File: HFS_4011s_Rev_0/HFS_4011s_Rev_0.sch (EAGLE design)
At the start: 63 parts, among them IC1 CP2104, J1 2X06, J2 2X12, J3 1X02, J4 microUSB, J5 1X02, J6 MOLEX_IGRID_15X2CONNECTOR, Q1 mmbt2222, Q2 mmbt2222, Q3 MMUN2133LT1G, Q4 BSS138, Q5 BSS138, SW2 KMR2, U1 TPS61090RSAR, U2 MCP73831T-2ACI/OT, U3 AD5693R, U4 LM3671MF-3.3/NOPB, X2 ESP32_WROOM32_SKINNY

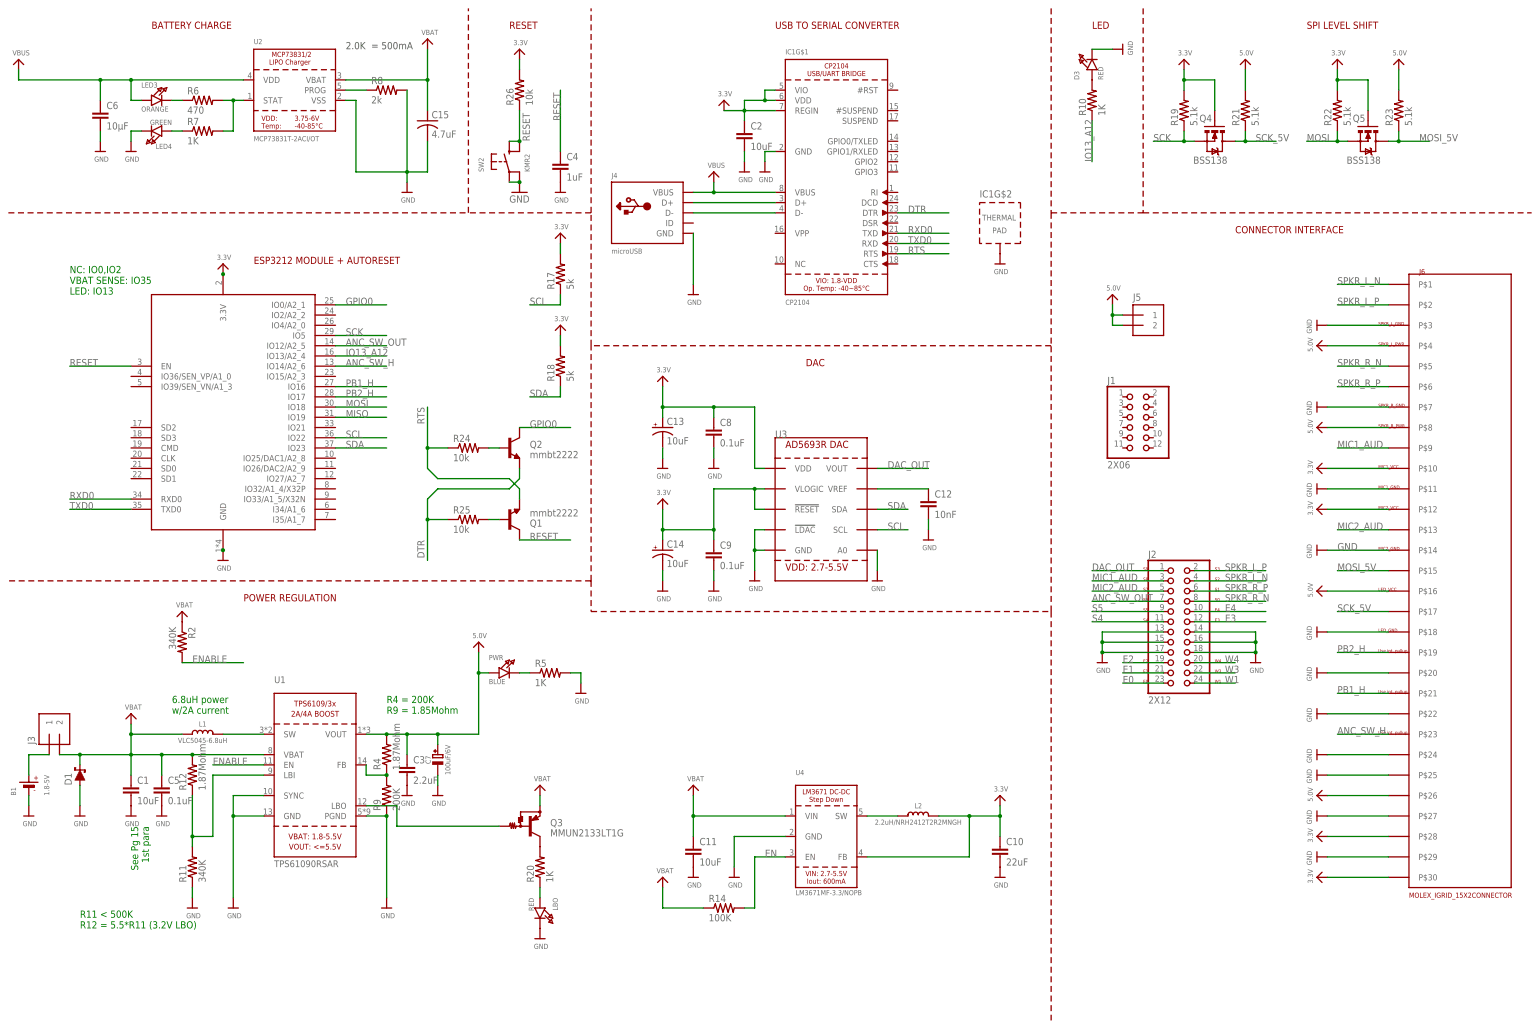
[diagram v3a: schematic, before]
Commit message: Renumbered components and fixing DRC errors.
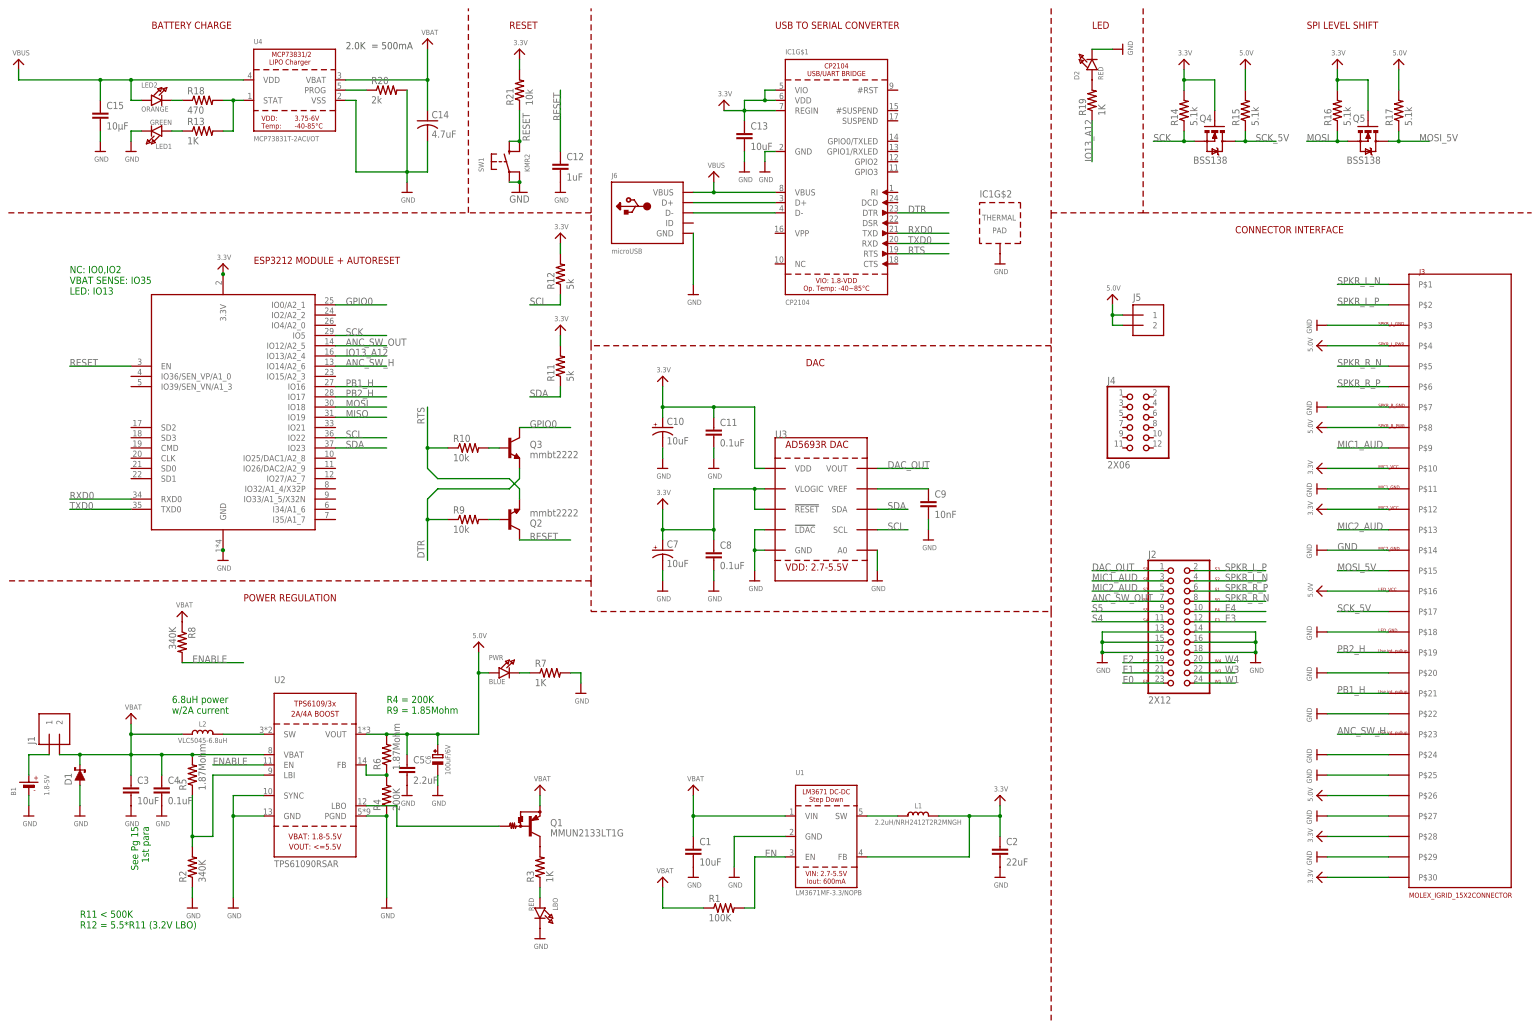
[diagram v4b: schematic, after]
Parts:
- removed R23: 5.1k, rcl:R-US_R0603
- removed R24, R25, R26: 10k, rcl:R-US_R0603
- added R1: 100K, rcl:R-US_R0603
- added R13, R3: 1K, rcl:R-US_R0603
- added R15: 5.1k, rcl:R-US_R0603
- C10: value 22uF -> 10uF; device rcl:C-EUC0603 -> SparkFun-Retired:10UF-TANT
- C11: value 10uF -> 0.1uF
- C12: value 10nF -> 1uF
- C13: device SparkFun-Retired:10UF-TANT -> rcl:C-EUC0603
- C14: value 10uF -> 4.7uF; device SparkFun-Retired:10UF-TANT -> rcl:C-USC1206
- C15: value 4.7uF -> 10µF; device rcl:C-USC1206 -> rcl:C-EUC0603
- C2: value 10uF -> 22uF
- C3: value 2.2uF -> 10uF
- C4: value 1uF -> 0.1uF
- C5: value 0.1uF -> 2.2uF
- C6: value 10µF -> 100uF/6V; device rcl:C-EUC0603 -> microbuilder:CAP_TANTALUMB/3528_REFLOW
- C7: value 100uF/6V -> 10uF; device microbuilder:CAP_TANTALUMB/3528_REFLOW -> SparkFun-Retired:10UF-TANT
- C9: value 0.1uF -> 10nF
- J1: value 2X06 -> 1X02; device HFS4011sCustom:2X06 -> HFS4011sCustom:1X02
- J3: value 1X02 -> MOLEX_IGRID_15X2CONNECTOR; device HFS4011sCustom:1X02 -> HFS4011sCustom:MOLEX_IGRID_15X2CONNECTOR
- J4: value microUSB -> 2X06; device microbuilder:USBMICRO_20329 -> HFS4011sCustom:2X06
- J6: value MOLEX_IGRID_15X2CONNECTOR -> microUSB; device HFS4011sCustom:MOLEX_IGRID_15X2CONNECTOR -> microbuilder:USBMICRO_20329
- L1: value VLC5045-6.8uH -> 2.2uH/NRH2412T2R2MNGH; device microbuilder:INDUCTORTDK_VLC5045 -> microbuilder:INDUCTORNRH2412T
- L2: value 2.2uH/NRH2412T2R2MNGH -> VLC5045-6.8uH; device microbuilder:INDUCTORNRH2412T -> microbuilder:INDUCTORTDK_VLC5045
- Q1: value mmbt2222 -> MMUN2133LT1G; device SparkFun:TRANSISTOR_NPNSOT23-3 -> transistor:MUN2114T1-PNP_DRIVER-SC59-BEC
- Q3: value MMUN2133LT1G -> mmbt2222; device transistor:MUN2114T1-PNP_DRIVER-SC59-BEC -> SparkFun:TRANSISTOR_NPNSOT23-3
- R10: value 1K -> 10k
- R11: value 340K -> 5k
- R12: value 1.87Mohm -> 5k
- R14: value 100K -> 5.1k
- R17: value 5k -> 5.1k
- R18: value 5k -> 470
- R19: value 5.1k -> 1K
- R20: value 1K -> 2k
- R21: value 5.1k -> 10k
- R4: value 1.87Mohm -> 200K
- R5: value 1K -> 1.87Mohm
- R6: value 470 -> 1.87Mohm
- R8: value 2k -> 340K
- R9: value 200K -> 10k
- U1: value TPS61090RSAR -> LM3671MF-3.3/NOPB; device microbuilder:VREG_TPS6103X -> microbuilder:VREG_LM3671
- U2: value MCP73831T-2ACI/OT -> TPS61090RSAR; device microbuilder:MCP73831/2 -> microbuilder:VREG_TPS6103X
- U4: value LM3671MF-3.3/NOPB -> MCP73831T-2ACI/OT; device microbuilder:VREG_LM3671 -> microbuilder:MCP73831/2
- renumbered D3 to D2, LED3 to LED2, LED4 to LED1, R22 to R16, SW2 to SW1, X2 to X1
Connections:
- net 3.3V: now also C10.+, C11.1, C13.1, C7.+, J3.P$10, J3.P$12, J3.P$28, J3.P$30, L1.2, R11.2, R12.2, R14.2, R21.2, U1.FB; no longer C10.1, C13.+, C14.+, C9.1, J6.P$10, J6.P$12, J6.P$28, J6.P$30, L2.2, R17.2, R18.2, R19.2, R26.2, U4.FB
- net 5.0V: now also C5.1, C6.+, J3.P$16, J3.P$26, J3.P$4, J3.P$8, R15.2, R17.2, R6.2, U2.VOUT; no longer C3.1, C7.+, J6.P$16, J6.P$26, J6.P$4, J6.P$8, R21.2, R23.2, R4.2, U1.VOUT
- net ANC_SW_H: now also J3.P$23; no longer J6.P$23
- net DTR: now also Q3.E, R9.1; no longer Q2.E, R25.1
- net EN: now also R1.2, U1.EN; no longer R14.2, U4.EN
- net ENABLE: now also R8.2, U2.EN; no longer R2.2, U1.EN
- net GND: now also C10.-, C13.2, C14.2, C6.-, J3.P$11, J3.P$14, J3.P$18, J3.P$20, J3.P$22, J3.P$24, J3.P$25, J3.P$27, J3.P$29, J3.P$3, J3.P$7, J6.GND, R2.1, R20.2, R4.1, R7.2, U2.GND, U2.PGND, U2.SYNC, U4.VSS; no longer C10.2, C13.-, C14.-, C6.2, J4.GND, J6.P$11, J6.P$14, J6.P$18, J6.P$20, J6.P$22, J6.P$24, J6.P$25, J6.P$27, J6.P$29, J6.P$3, J6.P$7, R11.1, R5.2, R8.2, R9.1, U1.PGND, U1.SYNC, U2.VSS, U4.GND
- net GPIO0: now also Q3.C; no longer Q2.C
- net IO13_A12: now also R19.1; no longer R10.1
- net LBO: now also Q1.B, U2.LBO; no longer Q3.B, U1.LBO
- net MIC1_AUD: now also J3.P$9; no longer J6.P$9
- net MIC2_AUD: now also J3.P$13; no longer J6.P$13
- net MOSI_5V: now also J3.P$15, R17.1; no longer J6.P$15, R23.1
- net N$1: now also R18.1; no longer R6.1
- net N$10: now also R7.1; no longer R5.1
- net N$11: now also R4.2, R6.1, U2.FB; no longer R4.1, R9.2, U1.FB
- net N$12: now also Q2.B, R9.2; no longer Q1.B, R25.2
- net N$13: now also Q3.B, R10.2; no longer Q2.B, R24.2
- net N$14: now also R3.1; no longer R20.1
- net N$15: now also Q1.C, R3.2; no longer Q3.C, R20.2
- net N$16: now also J1.1; no longer J3.1
- net N$17: now also L1.1, U1.SW; no longer L2.1, U4.SW
- net N$2: now also J6.D+; no longer J4.D+
- net N$20: now also C9.1; no longer C12.1
- net N$3: now also L2.2, U2.SW; no longer L1.2, U1.SW
- net N$4: now also R2.2, R5.1, U2.LBI; no longer R11.2, R12.1, U1.LBI
- net N$5: now also R19.2; no longer R10.2
- net N$6: now also J6.D-; no longer J4.D-
- net N$7: now also R13.2, R18.2, U4.STAT; no longer R6.2, R7.2, U2.STAT
- net N$8: now also R20.1, U4.PROG; no longer R8.1, U2.PROG
- net N$9: now also R13.1; no longer R7.1
- net PB1_H: now also J3.P$21; no longer J6.P$21
- net PB2_H: now also J3.P$19; no longer J6.P$19
- net RESET: now also C12.1, Q2.C, R21.1; no longer C4.1, Q1.C, R26.1
- net RTS: now also Q2.E, R10.1; no longer Q1.E, R24.1
- net SCK: now also R14.1; no longer R19.1
- net SCK_5V: now also J3.P$17, R15.1; no longer J6.P$17, R21.1
- net SCL: now also R12.1; no longer R17.1
- net SDA: now also R11.1; no longer R18.1
- net SPKR_L_N: now also J3.P$1; no longer J6.P$1
- net SPKR_L_P: now also J3.P$2; no longer J6.P$2
- net SPKR_R_N: now also J3.P$5; no longer J6.P$5
- net SPKR_R_P: now also J3.P$6; no longer J6.P$6
- net VBAT: now also C14.1, C3.1, C4.1, J1.2, L2.1, Q1.E, R1.1, R5.2, R8.1, U1.VIN, U4.VBAT; no longer C11.1, C15.1, C5.1, J3.2, L1.1, Q3.E, R12.2, R14.1, R2.1, U1.VBAT, U4.VIN
- net VBUS: now also C15.1, J6.VBUS, U4.VDD; no longer C6.1, J4.VBUS, U2.VDD
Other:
- moved on the sheet: C1, C11, C12, C15, C2, C3, C4, C5, C8, C9, L1, L2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

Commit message: Finished adding all silkscreen text. Got rid of some clearance errors. Seems like everything is set for fab.
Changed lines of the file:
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@@
 <grid distance="0.1" unitdist="inch" unit="inch" style="lines" multiple="1" display="no" altdistance="0.01" altunitdist="inch" altunit="inch"/>
 <layers>
-<layer number="1" name="Top" color="4" fill="1" visible="yes" active="no"/>
-<layer number="2" name="Route2" color="1" fill="3" visible="yes" active="no"/>
-<layer number="3" name="Route3" color="4" fill="3" visible="yes" active="no"/>
-<layer number="4" name="Route4" color="1" fill="4" visible="yes" active="no"/>
-<layer number="5" name="Route5" color="4" fill="4" visible="yes" active="no"/>
-<layer number="6" name="Route6" color="1" fill="8" visible="yes" active="no"/>
-<layer number="7" name="Route7" color="4" fill="8" visible="yes" active="no"/>
-<layer number="8" name="Route8" color="1" fill="2" visible="yes" active="no"/>
-<layer number="9" name="Route9" color="4" fill="2" visible="yes" active="no"/>
-<layer number="10" name="Route10" color="1" fill="7" visible="yes" active="no"/>
-<layer number="11" name="Route11" color="4" fill="7" visible="yes" active="no"/>
-<layer number="12" name="Route12" color="1" fill="5" visible="yes" active="no"/>
-<layer number="13" name="Route13" color="4" fill="5" visible="yes" active="no"/>
-<layer number="14" name="Route14" color="1" fill="6" visible="yes" active="no"/>
-<layer number="15" name="Route15" color="4" fill="6" visible="yes" active="no"/>
-<layer number="16" name="Bottom" color="1" fill="1" visible="yes" active="no"/>
-<layer number="17" name="Pads" color="2" fill="1" visible="yes" active="no"/>
-<layer number="18" name="Vias" color="2" fill="1" visible="yes" active="no"/>
-<layer number="19" name="Unrouted" color="6" fill="1" visible="yes" active="no"/>
-<layer number="20" name="Dimension" color="24" fill="1" visible="yes" active="no"/>
-<layer number="21" name="tPlace" color="7" fill="1" visible="yes" active="no"/>
-<layer number="22" name="bPlace" color="7" fill="1" visible="yes" active="no"/>
-<layer number="23" name="tOrigins" color="15" fill="1" visible="yes" active="no"/>
-<layer number="24" name="bOrigins" color="15" fill="1" visible="yes" active="no"/>
-<layer number="25" name="tNames" color="7" fill="1" visible="yes" active="no"/>
-<layer number="26" name="bNames" color="7" fill="1" visible="yes" active="no"/>
-<layer number="27" name="tValues" color="7" fill="1" visible="yes" active="no"/>
-<layer number="28" name="bValues" color="7" fill="1" visible="yes" active="no"/>
+<layer number="1" name="Top" color="4" fill="1" visible="no" active="no"/>
+<layer number="2" name="Route2" color="1" fill="3" visible="no" active="no"/>
+<layer number="3" name="Route3" color="4" fill="3" visible="no" active="no"/>
+<layer number="4" name="Route4" color="1" fill="4" visible="no" active="no"/>
+<layer number="5" name="Route5" color="4" fill="4" visible="no" active="no"/>
+<layer number="6" name="Route6" color="1" fill="8" visible="no" active="no"/>
+<layer number="7" name="Route7" color="4" fill="8" visible="no" active="no"/>
+<layer number="8" name="Route8" color="1" fill="2" visible="no" active="no"/>
+<layer number="9" name="Route9" color="4" fill="2" visible="no" active="no"/>
+<layer number="10" name="Route10" color="1" fill="7" visible="no" active="no"/>
+<layer number="11" name="Route11" color="4" fill="7" visible="no" active="no"/>
+<layer number="12" name="Route12" color="1" fill="5" visible="no" active="no"/>
+<layer number="13" name="Route13" color="4" fill="5" visible="no" active="no"/>
+<layer number="14" name="Route14" color="1" fill="6" visible="no" active="no"/>
+<layer number="15" name="Route15" color="4" fill="6" visible="no" active="no"/>
+<layer number="16" name="Bottom" color="1" fill="1" visible="no" active="no"/>
+<layer number="17" name="Pads" color="2" fill="1" visible="no" active="no"/>
+<layer number="18" name="Vias" color="2" fill="1" visible="no" active="no"/>
+<layer number="19" name="Unrouted" color="6" fill="1" visible="no" active="no"/>
+<layer number="20" name="Dimension" color="24" fill="1" visible="no" active="no"/>
+<layer number="21" name="tPlace" color="7" fill="1" visible="no" active="no"/>
+<layer number="22" name="bPlace" color="7" fill="1" visible="no" active="no"/>
+<layer number="23" name="tOrigins" color="15" fill="1" visible="no" active="no"/>
+<layer number="24" name="bOrigins" color="15" fill="1" visible="no" active="no"/>
+<layer number="25" name="tNames" color="7" fill="1" visible="no" active="no"/>
+<layer number="26" name="bNames" color="7" fill="1" visible="no" active="no"/>
+<layer number="27" name="tValues" color="7" fill="1" visible="no" active="no"/>
+<layer number="28" name="bValues" color="7" fill="1" visible="no" active="no"/>
 <layer number="29" name="tStop" color="7" fill="3" visible="no" active="no"/>
 <layer number="30" name="bStop" color="7" fill="6" visible="no" active="no"/>
@@
 <layer number="35" name="tGlue" color="7" fill="4" visible="no" active="no"/>
 <layer number="36" name="bGlue" color="7" fill="5" visible="no" active="no"/>
-<layer number="37" name="tTest" color="7" fill="1" visible="yes" active="no"/>
-<layer number="38" name="bTest" color="7" fill="1" visible="yes" active="no"/>
+<layer number="37" name="tTest" color="7" fill="1" visible="no" active="no"/>
+<layer number="38" name="bTest" color="7" fill="1" visible="no" active="no"/>
 <layer number="39" name="tKeepout" color="4" fill="11" visible="no" active="no"/>
 <layer number="40" name="bKeepout" color="1" fill="11" visible="no" active="no"/>
@@
 <layer number="44" name="Drills" color="7" fill="1" visible="no" active="no"/>
 <layer number="45" name="Holes" color="7" fill="1" visible="no" active="no"/>
-<layer number="46" name="Milling" color="3" fill="1" visible="yes" active="no"/>
-<layer number="47" name="Measures" color="7" fill="1" visible="yes" active="no"/>
-<layer number="48" name="Document" color="7" fill="1" visible="yes" active="no"/>
-<layer number="49" name="Reference" color="7" fill="1" visible="yes" active="no"/>
-<layer number="50" name="dxf" color="7" fill="1" visible="yes" active="no"/>
-<layer number="51" name="tDocu" color="7" fill="1" visible="yes" active="no"/>
-<layer number="52" name="bDocu" color="7" fill="1" visible="yes" active="no"/>
-<layer number="53" name="tGND_GNDA" color="7" fill="9" visible="yes" active="no"/>
-<layer number="54" name="bGND_GNDA" color="1" fill="9" visible="yes" active="no"/>
-<layer number="56" name="wert" color="7" fill="1" visible="yes" active="no"/>
-<layer number="57" name="tCAD" color="7" fill="1" visible="yes" active="no"/>
-<layer number="59" name="tCarbon" color="7" fill="1" visible="yes" active="no"/>
-<layer number="60" name="bCarbon" color="7" fill="1" visible="yes" active="no"/>
+<layer number="46" name="Milling" color="3" fill="1" visible="no" active="no"/>
+<layer number="47" name="Measures" color="7" fill="1" visible="no" active="no"/>
+<layer number="48" name="Document" color="7" fill="1" visible="no" active="no"/>
+<layer number="49" name="Reference" color="7" fill="1" visible="no" active="no"/>
+<layer number="50" name="dxf" color="7" fill="1" visible="no" active="no"/>
+<layer number="51" name="tDocu" color="7" fill="1" visible="no" active="no"/>
+<layer number="52" name="bDocu" color="7" fill="1" visible="no" active="no"/>
+<layer number="53" name="tGND_GNDA" color="7" fill="9" visible="no" active="no"/>
+<layer number="54" name="bGND_GNDA" color="1" fill="9" visible="no" active="no"/>
+<layer number="56" name="wert" color="7" fill="1" visible="no" active="no"/>
+<layer number="57" name="tCAD" color="7" fill="1" visible="no" active="no"/>
+<layer number="59" name="tCarbon" color="7" fill="1" visible="no" active="no"/>
+<layer number="60" name="bCarbon" color="7" fill="1" visible="no" active="no"/>
 <layer number="88" name="SimResults" color="9" fill="1" visible="yes" active="yes"/>
 <layer number="89" name="SimProbes" color="9" fill="1" visible="yes" active="yes"/>
@@
 <part name="R16" library="rcl" library_urn="urn:adsk.eagle:library:334" deviceset="R-US_" device="R0603" package3d_urn="urn:adsk.eagle:package:23555/2" value="5.1k"/>
 <part name="R17" library="rcl" library_urn="urn:adsk.eagle:library:334" deviceset="R-US_" device="R0603" package3d_urn="urn:adsk.eagle:package:23555/2" value="5.1k"/>
-<part name="J3" library="HFS4011sCustom" deviceset="MOLEX_IGRID_15X2CONNECTOR" device=""/>
+<part name="J3" library="HFS4011sCustom" deviceset="MOLEX_IGRID_15X2CONNECTOR" device="" value=""/>
 <part name="U$63" library="microbuilder" deviceset="GND" device=""/>
 <part name="C14" library="rcl" library_urn="urn:adsk.eagle:library:334" deviceset="C-US" device="C1206" package3d_urn="urn:adsk.eagle:package:23618/2" value="4.7uF"/>
@@
 </sheet>
 </sheets>
+<errors>
+</errors>
 </schematic>
 </drawing>
